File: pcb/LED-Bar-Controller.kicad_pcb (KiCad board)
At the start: 4 copper layers, 46 x 44 mm, 38 parts, among them J1 Conn_01x03, J2 USB_C, J3 Serial, Q1 AO3400A, Q2 AO3400A, SW1 Power, SW2 Color, SW3 Bright-, SW4 Bright+, U1 ESP32-WROOM-32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

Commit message: fix: switch WW and CW positions
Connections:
- J1 pad 2: /CW -> /WW
- J1 pad 3: /WW -> /CW
- Q1 pad 1: /Gcw -> /Gww
- Q1 pad 3: /CW -> /WW
- Q2 pad 1: /Gww -> /Gcw
- Q2 pad 3: /WW -> /CW
- R1 pad 1: /PWM_CW -> /PWM_WW
- R1 pad 2: /Gcw -> /Gww
- R2 pad 1: /PWM_CW -> /PWM_WW
- R3 pad 1: /PWM_WW -> /PWM_CW
- R3 pad 2: /Gww -> /Gcw
- R4 pad 1: /PWM_WW -> /PWM_CW
- U1 pad 30: /PWM_WW -> /PWM_CW
- U1 pad 31: /PWM_CW -> /PWM_WW
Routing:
- net /PWM_WW: track 5.63 -> 7.16 mm
- net /PWM_CW: track 7.16 -> 5.63 mm
- net /WW: track 3.32 -> 4.34 mm
- net /CW: track 4.34 -> 3.32 mm

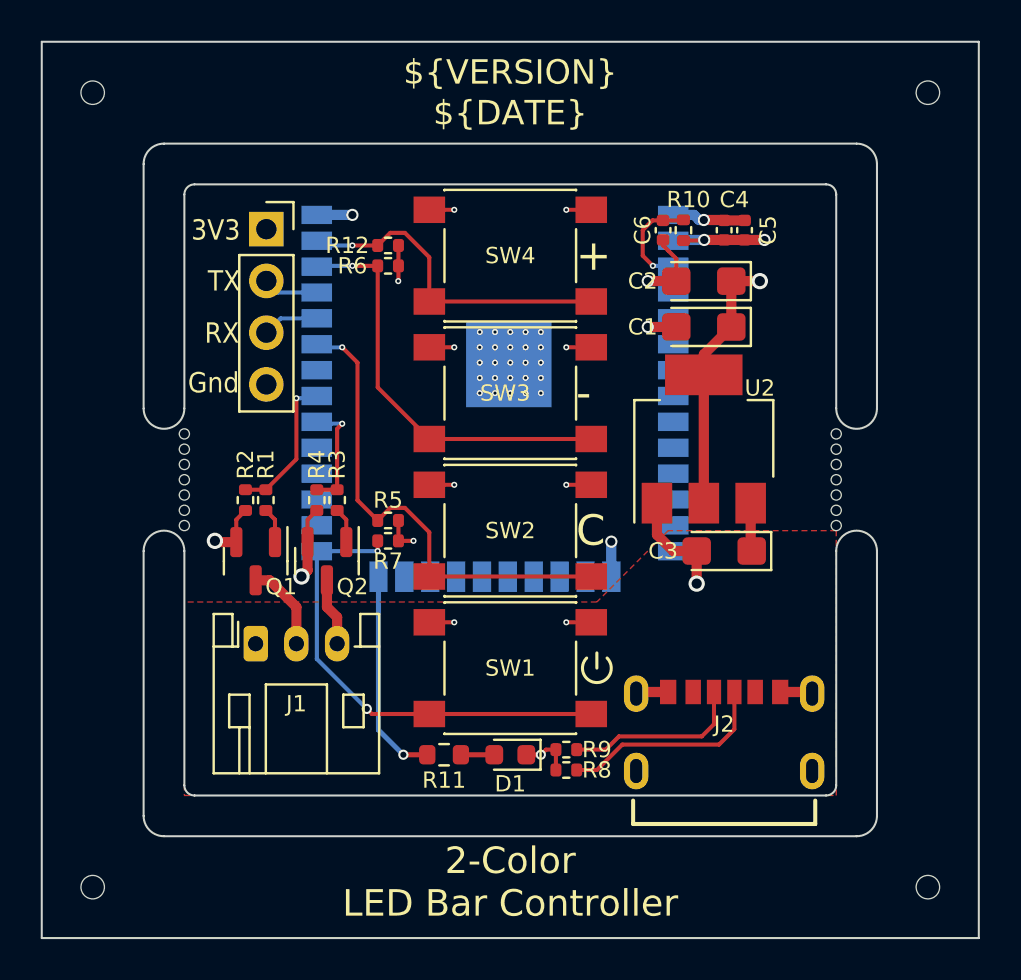
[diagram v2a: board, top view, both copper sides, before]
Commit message: feat: change button type
change buttons to type in JLCPCB basic library and change their positions
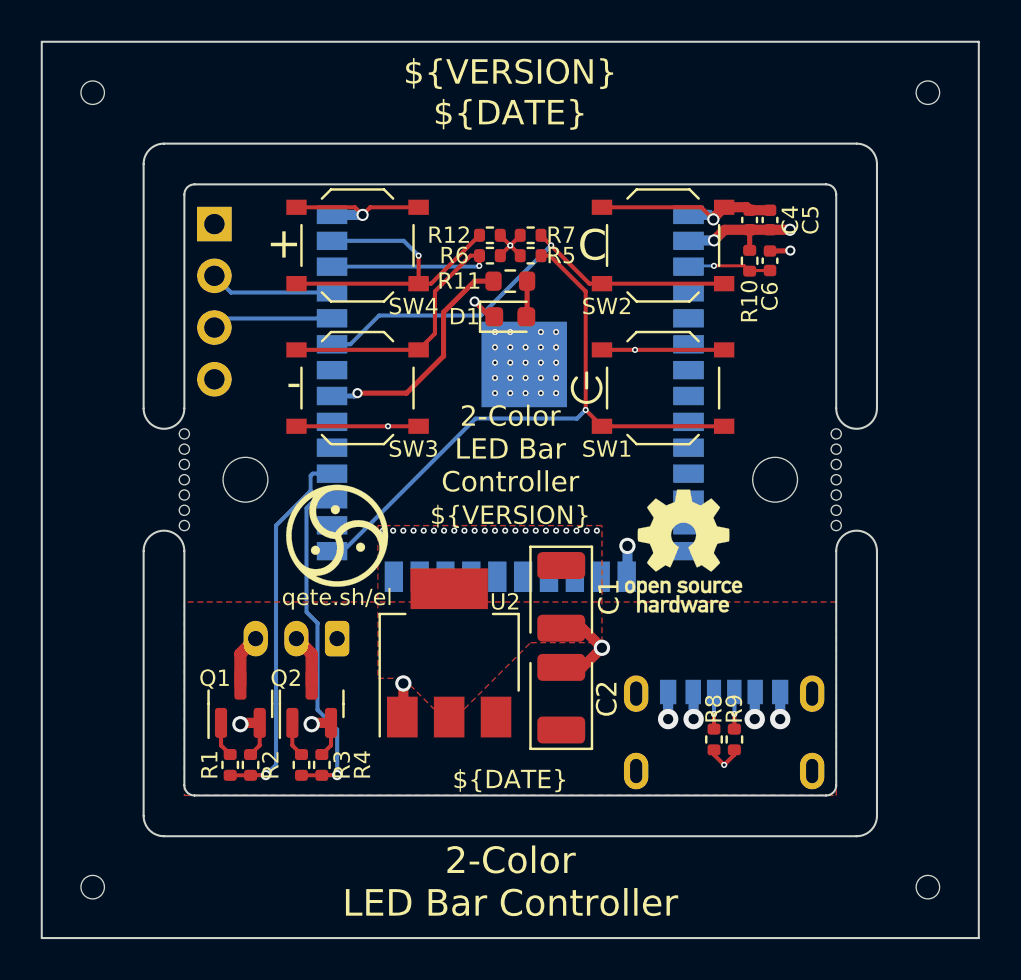
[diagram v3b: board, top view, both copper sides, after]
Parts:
- removed the C2 at (148.2, 90.2)
- added REF**: MountingHole_2.2mm_M2, MountingHole:MountingHole_2.2mm_M2, F.Cu at (125.8, 100.0)
- added REF**: MountingHole_2.2mm_M2, MountingHole:MountingHole_2.2mm_M2, F.Cu at (151.8, 100.0)
- C1: value 10u -> 100u; footprint Capacitor_Tantalum_SMD:CP_EIA-3216-18_Kemet-A -> Capacitor_Tantalum_SMD:CP_EIA-3528-21_Kemet-B
- C2: renamed from C3; value 10u -> 100u; footprint Capacitor_Tantalum_SMD:CP_EIA-3216-18_Kemet-A -> Capacitor_Tantalum_SMD:CP_EIA-3528-21_Kemet-B
- G***, REF**: moved to F.Cu
- J1, J2, J3: moved to B.Cu
- SW1, SW2, SW3, SW4: footprint Button_Switch_SMD:SW_Push_1P1T_NO_6x6mm_H9.5mm -> Button_Switch_SMD:SW_Push_1P1T_XKB_TS-1187A
- moved R11 23.5 mm to (138.8, 90.2)
- moved G*** 22.3 mm to (130.2, 102.8), turned to 0 degrees
- moved D1 21.5 mm to (138.8, 92.0), turned to 0 degrees
- moved U2 16.3 mm to (135.8, 108.5)
- moved SW2 15.9 mm to (146.2, 88.5)
- moved SW1 15.7 mm to (146.2, 95.5)
- moved R5 15.7 mm to (139.8, 88.0), turned to 0 degrees
- moved R7 15.7 mm to (139.8, 89.0), turned to 0 degrees
- moved REF** 15.0 mm to (147.2, 103.5), turned to 0 degrees
- moved C1 15.0 mm to (141.2, 105.8), turned to -90 degrees
- moved R1 13.1 mm to (125.0, 114.0), turned to 90 degrees
- moved R3 13.1 mm to (128.5, 114.0), turned to 90 degrees
- moved R2 13.0 mm to (126.0, 114.0), turned to 90 degrees
- moved R4 13.0 mm to (129.5, 114.0), turned to 90 degrees
- moved C2 10.8 mm to (141.2, 110.8), turned to 90 degrees
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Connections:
- Q1 pad 1: /Gww -> /Gcw
- Q1 pad 3: /WW -> /CW
- Q2 pad 1: /Gcw -> /Gww
- Q2 pad 3: /CW -> /WW
- R1 pad 1: /PWM_WW -> /PWM_CW
- R1 pad 2: /Gww -> /Gcw
- R2 pad 1: /PWM_WW -> /PWM_CW
- R3 pad 1: /PWM_CW -> /PWM_WW
- R3 pad 2: /Gcw -> /Gww
- R4 pad 1: /PWM_CW -> /PWM_WW
- U1 pad 24: /Status_LED -> unconnected-(U1-IO2-Pad24)
- U1 pad 27: unconnected-(U1-IO16-Pad27) -> /PWM_WW
- U1 pad 28: unconnected-(U1-IO17-Pad28) -> /PWM_CW
- U1 pad 30: /PWM_CW -> unconnected-(U1-IO18-Pad30)
- U1 pad 31: /PWM_WW -> /Status_LED
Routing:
- net /PWM_CW: track 5.63 -> 18.5 mm
- net +3V3: track 21.6 -> 9.03 mm, vias 5 -> 25
- net GND: track 39.5 -> 50.2 mm, vias 42 -> 38
- net /PWM_WW: track 7.16 -> 16.9 mm
- net /CC2: track 10.4 -> 1.82 mm, vias 0 -> 1
- net /SW_Power: track 23.4 -> 31.2 mm, vias 2 -> 1
- net /CC1: track 8.84 -> 1.82 mm, vias 0 -> 1
- net /TX: track 2.71 -> 6.11 mm
- net /RX: track 2.76 -> 5.96 mm
- net /WW: track 4.34 -> 2.57 mm
- net /SW_Color: track 23.9 -> 22.7 mm
- net /Status_LED: track 10.4 -> 11.5 mm
- net /EN: track 5.18 -> 4.14 mm
- net /CW: track 3.32 -> 2.57 mm
- net /SW_Bright-: track 20.5 -> 19.9 mm
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- added copper zone on F.Cu, net +3V3
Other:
- board text added: "G"
- board text removed: "${VERSION} ${DATE}"
- board text removed: "Gnd"
